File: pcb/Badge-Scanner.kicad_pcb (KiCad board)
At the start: 2 copper layers, 73 x 52 mm, 71 parts, among them J1 NFC-Module, J2 Serial, J3 I2C, J4 Micro_SD_Card_Det1, M1 Fan, Q1 AO3400A, Q2 AO3401A, Q3 AO3401A, Q5 AO3400A, Q6 AO3400A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

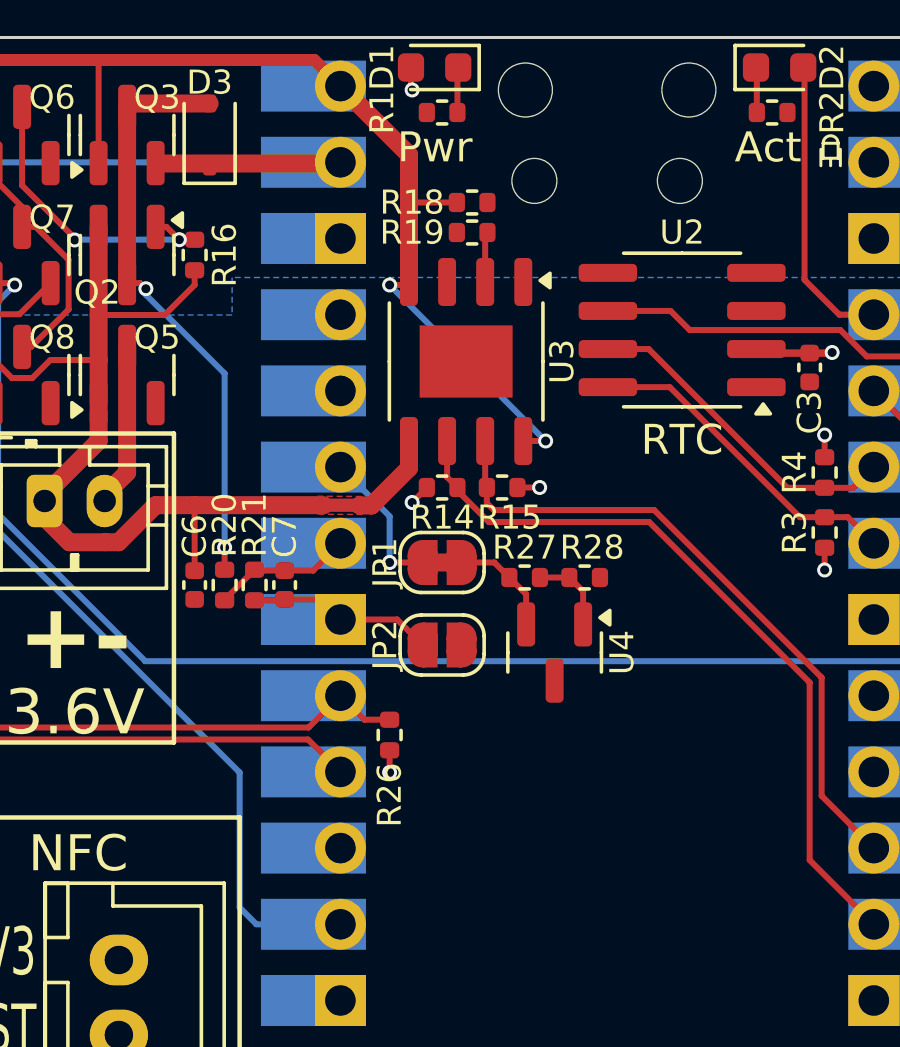
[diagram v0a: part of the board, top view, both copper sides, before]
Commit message: fix: add caps to delay startup of mcu
Sometimes the mcu does not boot correctly when usb gets connected while the system is off - most likely because the flash does not get enough power quick enough. Adding a startup delay for the 3V3 regulator and the mcu itself helps in my tests. This delays the boot by about half a second.
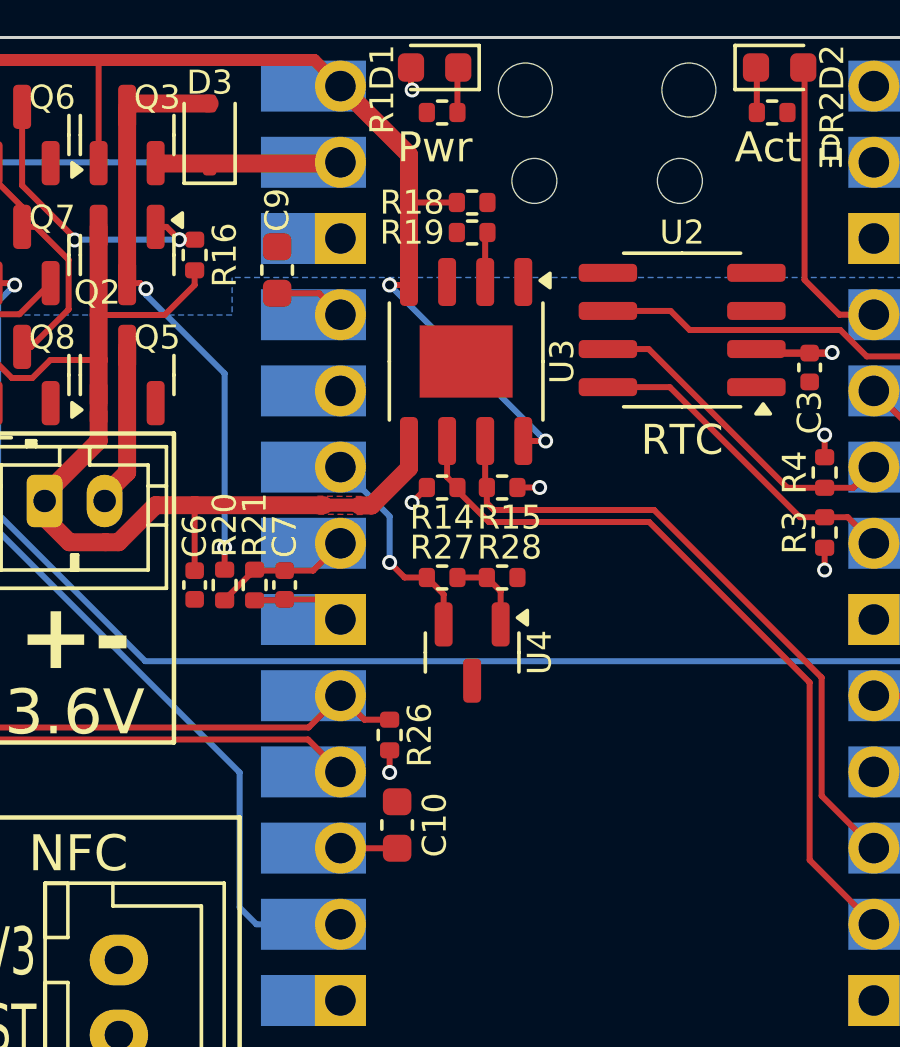
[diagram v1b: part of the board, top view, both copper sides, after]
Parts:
- removed JP1: VREF, Jumper:SolderJumper-2_P1.3mm_Bridged_RoundedPad1.0x1.5mm
- removed JP2: AGND, Jumper:SolderJumper-2_P1.3mm_Open_RoundedPad1.0x1.5mm
- added C10: 22u, Capacitor_SMD:C_0603_1608Metric, F.Cu at (118.0, 100.5)
- added C9: 22u, Capacitor_SMD:C_0603_1608Metric, F.Cu at (114.0, 82.0)
- moved R27 2.75 mm to (119.5, 92.2)
- moved R28 2.75 mm to (121.5, 92.2)
- moved U4 2.75 mm to (120.5, 94.8)
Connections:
- R27 pad 1: /3V_REF -> /ADC_VREF
- U1 pad 30: unconnected-(U1-RUN-Pad30) -> /RUN
- U1 pad 37: unconnected-(U1-3V3_EN-Pad37) -> /3V3_EN
- U4 pad 2: /3V_REF -> /ADC_VREF
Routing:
- net /3V_REF: track 3.59 -> 0.00 mm
- net GNDA: track 6.24 -> 3.15 mm
- net /3V3_EN: track 0.00 -> 2.41 mm
- net /ADC_VREF: track 4.96 -> 7.10 mm
- net /RUN: track 0.00 -> 1.89 mm

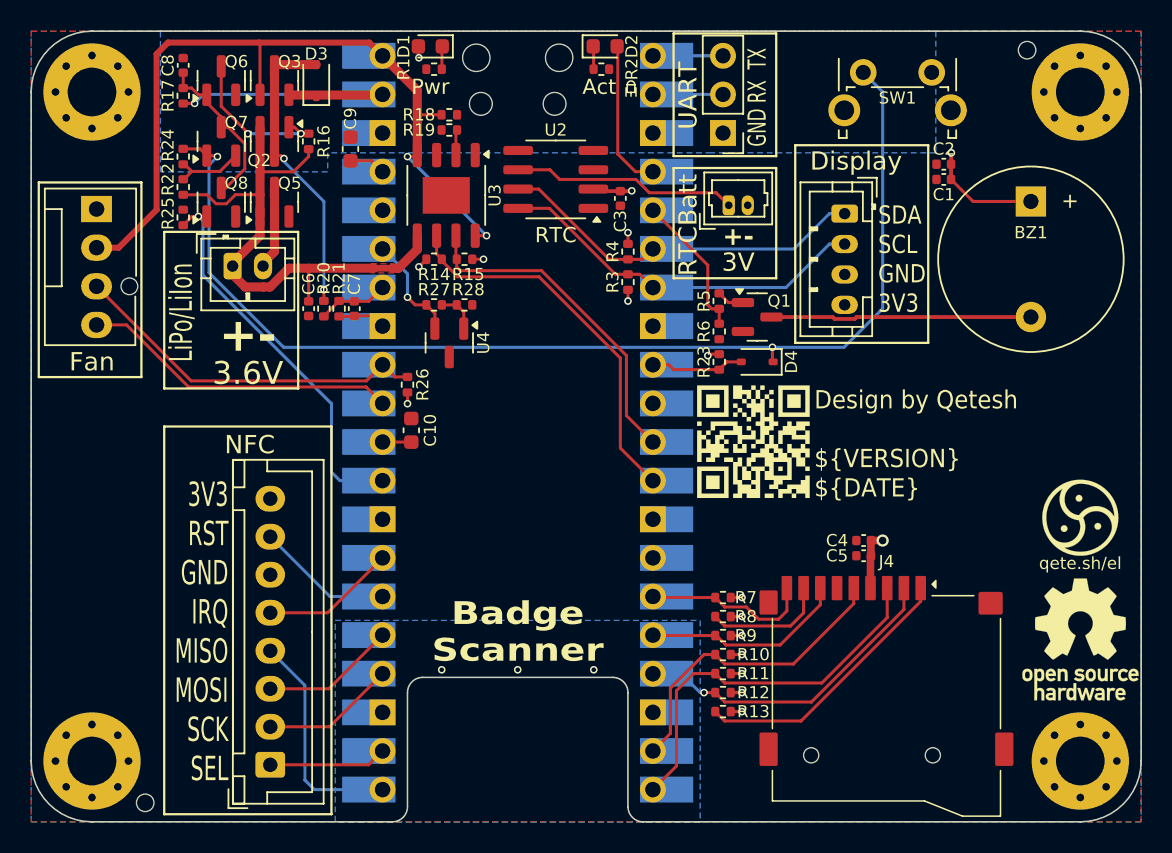
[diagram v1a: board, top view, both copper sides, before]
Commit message: feat: add reset button
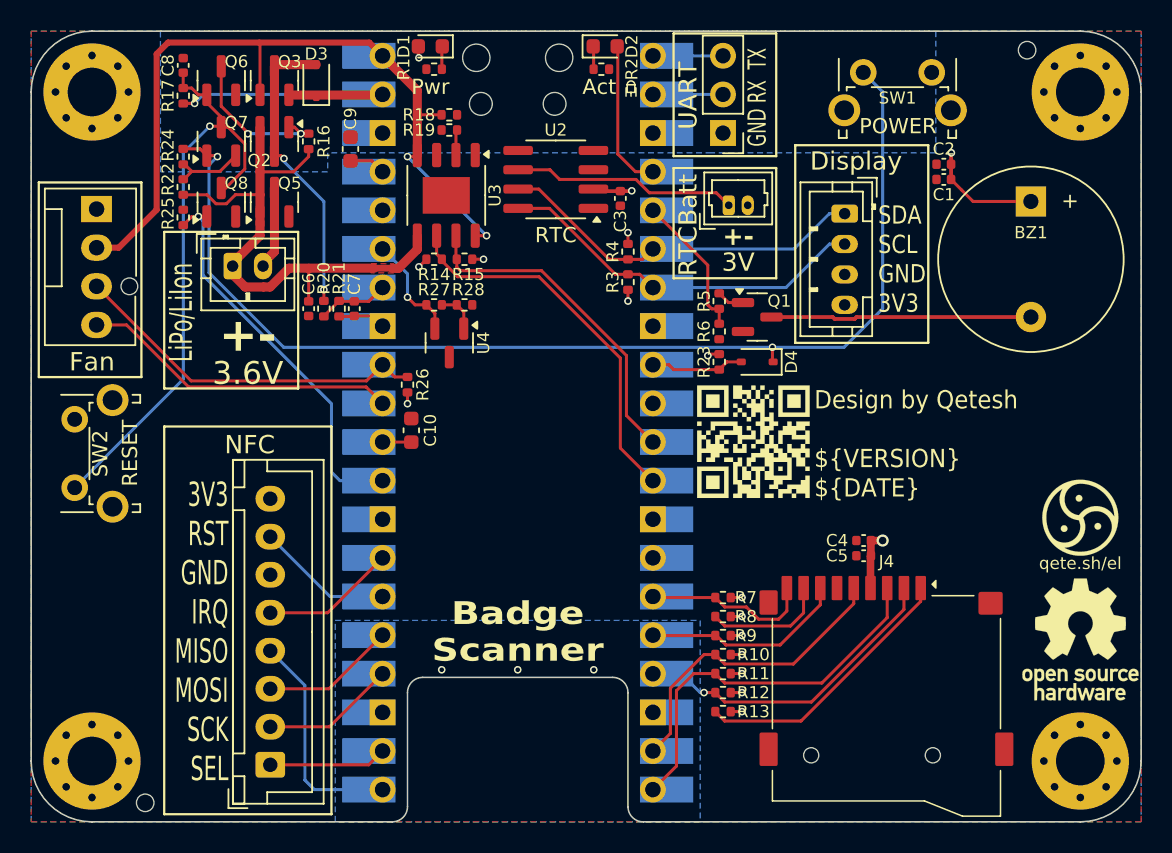
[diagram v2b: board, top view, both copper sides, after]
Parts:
- added SW2: Reset, Button_Switch_THT:SW_Tactile_SPST_Angled_PTS645Vx31-2LFS, F.Cu at (95.9, 104.3)
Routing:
- net /Battery Management/BattSw: track 11.0 -> 39.2 mm, vias 0 -> 1
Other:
- board text added: "POWER"
- board text added: "RESET"
